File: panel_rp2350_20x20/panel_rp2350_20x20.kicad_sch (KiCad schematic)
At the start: 0 parts

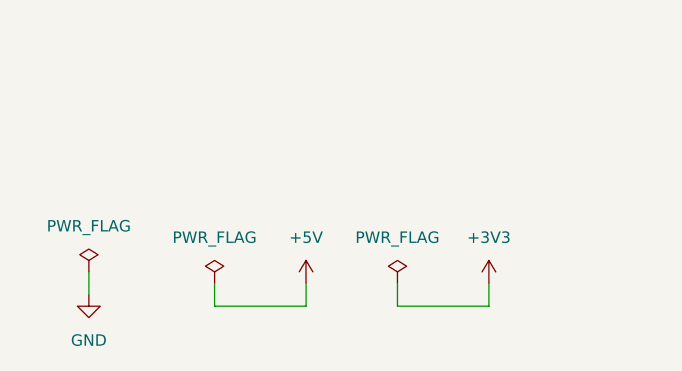
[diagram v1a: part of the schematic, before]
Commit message: Worked on rp2350 20x20 panel layout and routing.
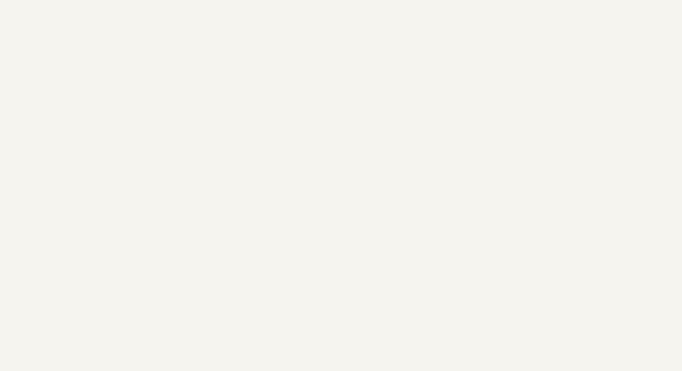
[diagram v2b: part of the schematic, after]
